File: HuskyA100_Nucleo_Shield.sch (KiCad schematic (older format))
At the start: 16 parts, among them CN10 HEADER_17x2, CN7 HEADER_10x2, CN8 HEADER_8x2, CN9 HEADER_15x2, J1 Conn_01x03, J2 Conn_01x03, J3 Conn_01x04, J4 Conn_01x04

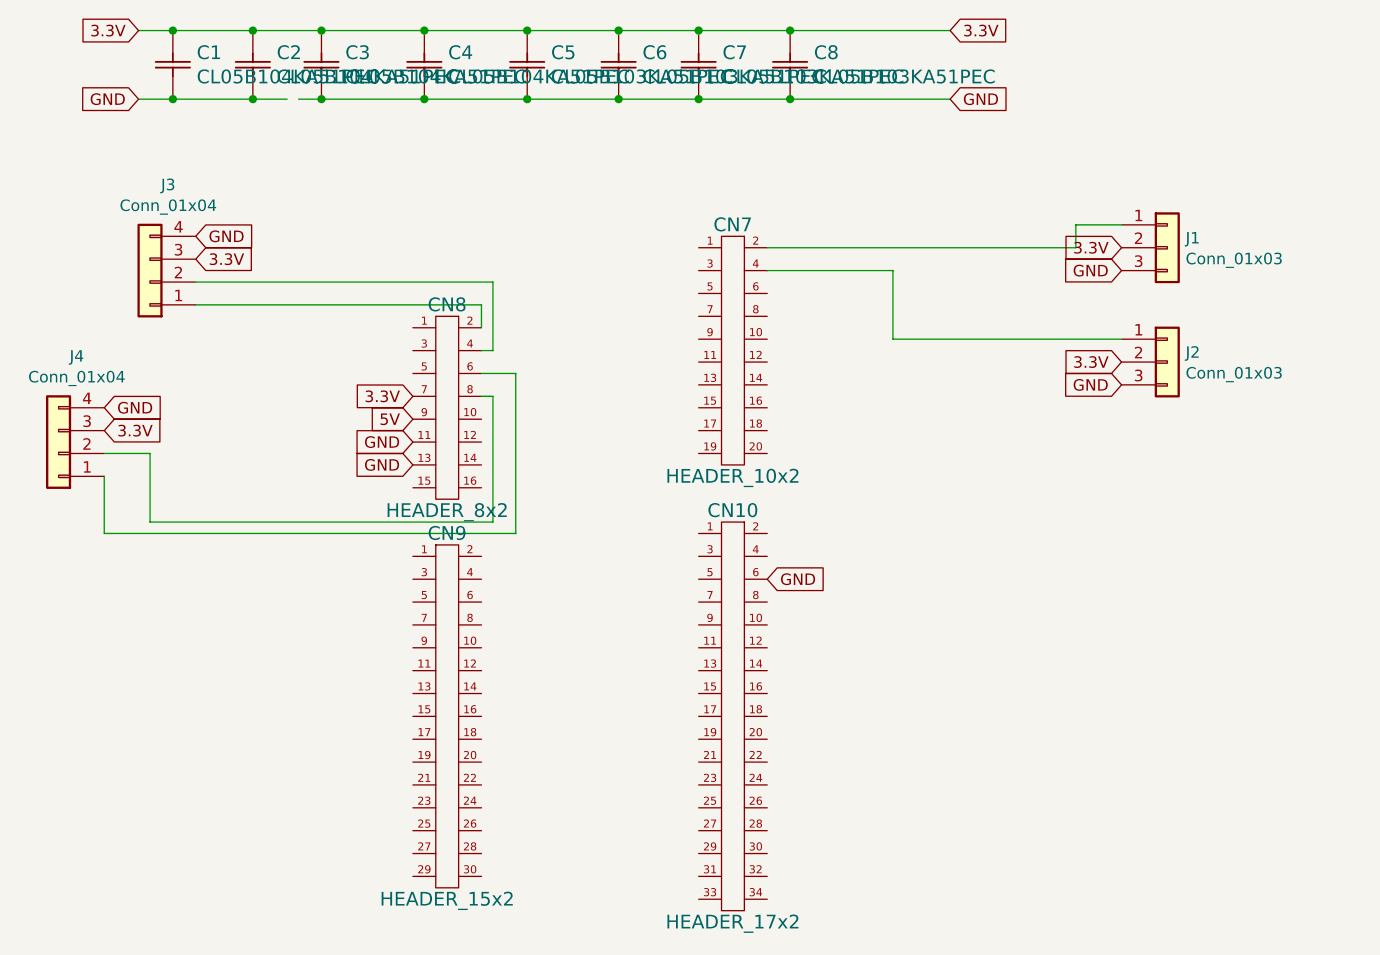
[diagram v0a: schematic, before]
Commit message: rerouted the pins to be correct in the schematic + deleted old traces
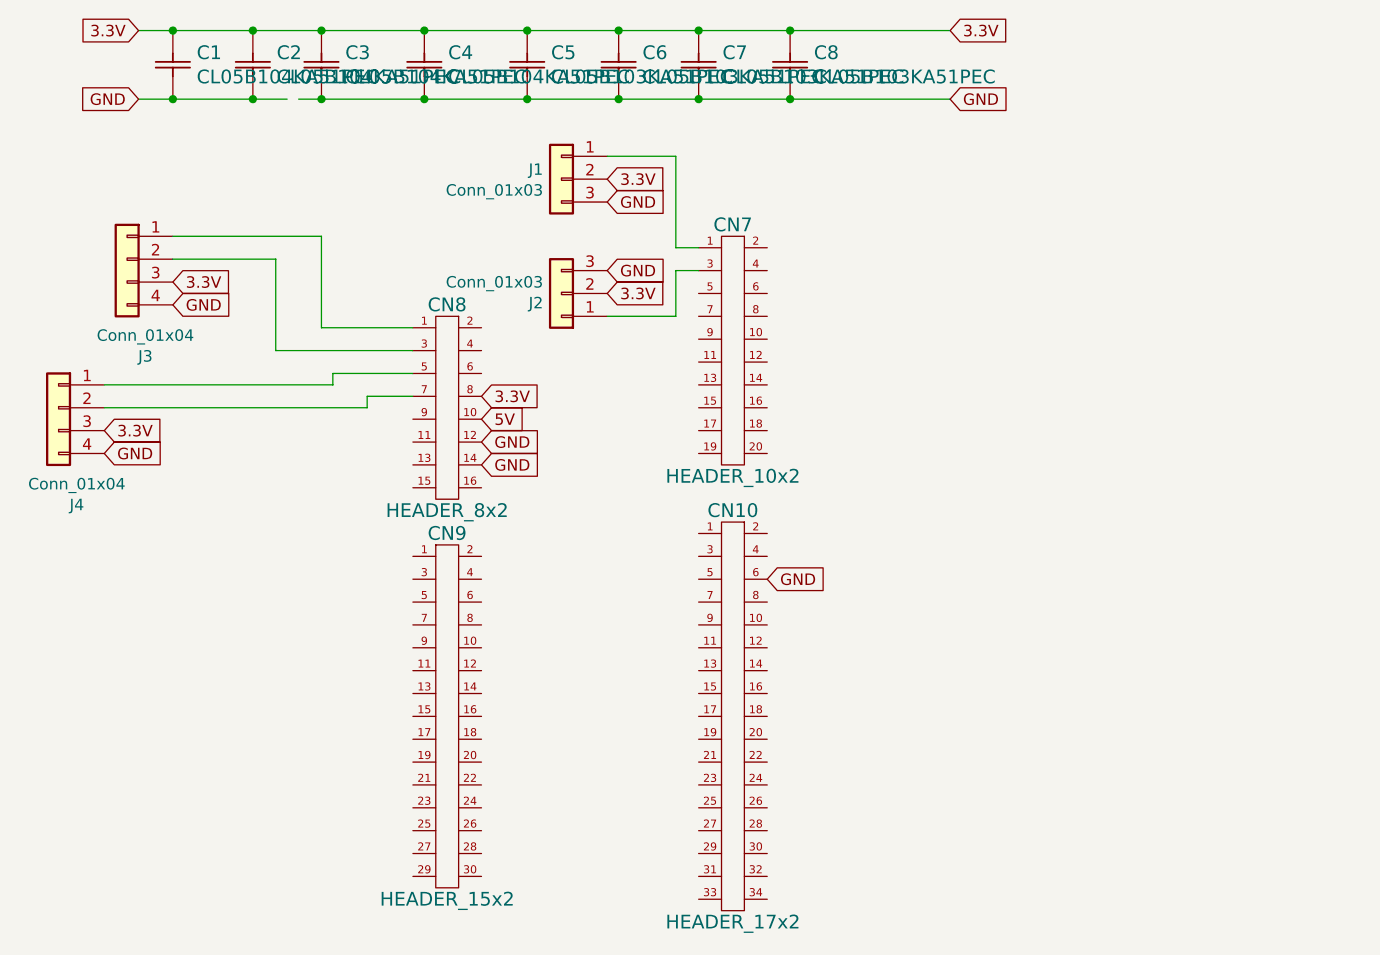
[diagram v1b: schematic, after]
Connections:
- wire segments 39 -> 37
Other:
- moved on the sheet: J1, J2, J3, J4
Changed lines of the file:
@@
 EESchema Schematic File Version 4
+LIBS:HuskyA100_Nucleo_Shield-cache
 EELAYER 26 0
 EELAYER END
@@
 L Connector_Generic:Conn_01x03 J1
 U 1 1 5C0735EF
-P 7450 3150
-F 0 "J1" H 7530 3192 50  0000 L CNN
-F 1 "Conn_01x03" H 7530 3101 50  0000 L CNN
-F 2 "Molex_Mini-Lock:Molex Mini-Lock Horizontal Header 3 circuit" H 7450 3150 50  0001 C CNN
-F 3 "~" H 7450 3150 50  0001 C CNN
-	1    7450 3150
-	1    0    0    -1
+P 4800 2850
+F 0 "J1" H 4880 2892 50  0000 L CNN
+F 1 "Conn_01x03" H 4880 2801 50  0000 L CNN
+F 2 "Molex_Mini-Lock:Molex Mini-Lock Horizontal Header 3 circuit" H 4800 2850 50  0001 C CNN
+F 3 "~" H 4800 2850 50  0001 C CNN
+	1    4800 2850
+	-1   0    0    -1
 $EndComp
 $Comp
 L Connector_Generic:Conn_01x03 J2
 U 1 1 5C0737C1
-P 7450 3650
-F 0 "J2" H 7530 3692 50  0000 L CNN
-F 1 "Conn_01x03" H 7530 3601 50  0000 L CNN
-F 2 "Molex_Mini-Lock:Molex Mini-Lock Horizontal Header 3 circuit" H 7450 3650 50  0001 C CNN
-F 3 "~" H 7450 3650 50  0001 C CNN
-	1    7450 3650
-	1    0    0    -1
+P 4800 3350
+F 0 "J2" H 4880 3392 50  0000 L CNN
+F 1 "Conn_01x03" H 4880 3301 50  0000 L CNN
+F 2 "Molex_Mini-Lock:Molex Mini-Lock Horizontal Header 3 circuit" H 4800 3350 50  0001 C CNN
+F 3 "~" H 4800 3350 50  0001 C CNN
+	1    4800 3350
+	-1   0    0    1
 $EndComp
 $Comp
 L Connector_Generic:Conn_01x04 J3
 U 1 1 5C073803
-P 3000 3300
-F 0 "J3" H 2920 2875 50  0000 C CNN
-F 1 "Conn_01x04" H 2920 2966 50  0000 C CNN
-F 2 "Molex_Mini-Lock:Molex Mini-Lock Horizontal Header 4 circuit" H 3000 3300 50  0001 C CNN
-F 3 "~" H 3000 3300 50  0001 C CNN
-	1    3000 3300
-	-1   0    0    1
+P 2900 3200
+F 0 "J3" H 2820 2775 50  0000 C CNN
+F 1 "Conn_01x04" H 2820 2866 50  0000 C CNN
+F 2 "Molex_Mini-Lock:Molex Mini-Lock Horizontal Header 4 circuit" H 2900 3200 50  0001 C CNN
+F 3 "~" H 2900 3200 50  0001 C CNN
+	1    2900 3200
+	-1   0    0    -1
 $EndComp
 $Comp
 L Connector_Generic:Conn_01x04 J4
 U 1 1 5C073BBE
-P 2600 4050
-F 0 "J4" H 2520 3625 50  0000 C CNN
-F 1 "Conn_01x04" H 2520 3716 50  0000 C CNN
-F 2 "Molex_Mini-Lock:Molex Mini-Lock Horizontal Header 4 circuit" H 2600 4050 50  0001 C CNN
-F 3 "~" H 2600 4050 50  0001 C CNN
-	1    2600 4050
-	-1   0    0    1
-$EndComp
-Wire Wire Line
-	4450 3500 4450 3400
-Wire Wire Line
-	4450 3400 3200 3400
-Wire Wire Line
-	4500 3600 4500 3300
-Wire Wire Line
-	4500 3300 3200 3300
-Wire Wire Line
-	4500 3600 4450 3600
-Wire Wire Line
-	4450 3700 4600 3700
-Wire Wire Line
-	4450 3800 4500 3800
-Wire Wire Line
-	3000 4050 2800 4050
-Wire Wire Line
-	2800 4150 2800 4400
-Wire Wire Line
-	3000 4050 3000 4350
-Wire Wire Line
-	5700 3150 7050 3150
-Wire Wire Line
-	7050 3150 7050 3050
-Wire Wire Line
-	7050 3050 7250 3050
-Wire Wire Line
-	7250 3550 6250 3550
-Wire Wire Line
-	6250 3550 6250 3250
-Wire Wire Line
-	6250 3250 5700 3250
-Wire Wire Line
-	4500 4350 4500 3800
-Wire Wire Line
-	3000 4350 4500 4350
-Wire Wire Line
-	4600 4400 4600 3700
-Wire Wire Line
-	2800 4400 4600 4400
-Text GLabel 4150 3900 0    50   Input ~ 0
+P 2600 3850
+F 0 "J4" H 2520 3425 50  0000 C CNN
+F 1 "Conn_01x04" H 2520 3516 50  0000 C CNN
+F 2 "Molex_Mini-Lock:Molex Mini-Lock Horizontal Header 4 circuit" H 2600 3850 50  0001 C CNN
+F 3 "~" H 2600 3850 50  0001 C CNN
+	1    2600 3850
+	-1   0    0    -1
+$EndComp
+Text GLabel 4450 3900 2    50   Input ~ 0
 5V
-Text GLabel 4150 4000 0    50   Input ~ 0
-GND
-Text GLabel 4150 4100 0    50   Input ~ 0
-GND
-Text GLabel 4150 3800 0    50   Input ~ 0
+Text GLabel 4450 4000 2    50   Input ~ 0
+GND
+Text GLabel 4450 4100 2    50   Input ~ 0
+GND
+Text GLabel 4450 3800 2    50   Input ~ 0
 3.3V
 Text GLabel 2800 3950 2    50   Input ~ 0
 3.3V
-Text GLabel 3200 3200 2    50   Input ~ 0
-3.3V
-Text GLabel 7250 3750 0    50   Input ~ 0
-GND
-Text GLabel 7250 3250 0    50   Input ~ 0
-GND
-Text GLabel 7250 3150 0    50   Input ~ 0
-3.3V
-Text GLabel 7250 3650 0    50   Input ~ 0
-3.3V
-Text GLabel 3200 3100 2    50   Input ~ 0
-GND
-Text GLabel 2800 3850 2    50   Input ~ 0
+Text GLabel 3100 3300 2    50   Input ~ 0
+3.3V
+Text GLabel 5000 3250 2    50   Input ~ 0
+GND
+Text GLabel 5000 3350 2    50   Input ~ 0
+3.3V
+Text GLabel 3100 3400 2    50   Input ~ 0
+GND
+Text GLabel 2800 4050 2    50   Input ~ 0
 GND
 Text GLabel 5700 4600 2    50   Input ~ 0
@@
 Wire Wire Line
 	5800 2500 6500 2500
+Wire Wire Line
+	2800 3750 3800 3750
+Wire Wire Line
+	3800 3700 4150 3700
+Wire Wire Line
+	3950 3800 4150 3800
+Wire Wire Line
+	2800 3850 3950 3850
+Wire Wire Line
+	3950 3800 3950 3850
+Wire Wire Line
+	3800 3700 3800 3750
+Wire Wire Line
+	3100 3200 3550 3200
+Wire Wire Line
+	3550 3200 3550 3600
+Wire Wire Line
+	3550 3600 4150 3600
+Wire Wire Line
+	4150 3500 3750 3500
+Wire Wire Line
+	3750 3500 3750 3100
+Wire Wire Line
+	3750 3100 3100 3100
+Text GLabel 5000 2850 2    50   Input ~ 0
+3.3V
+Text GLabel 5000 2950 2    50   Input ~ 0
+GND
+Wire Wire Line
+	5000 2750 5300 2750
+Wire Wire Line
+	5300 2750 5300 3150
+Wire Wire Line
+	5300 3150 5400 3150
+Wire Wire Line
+	5000 3450 5300 3450
+Wire Wire Line
+	5300 3450 5300 3250
+Wire Wire Line
+	5300 3250 5400 3250
 $EndSCHEMATC

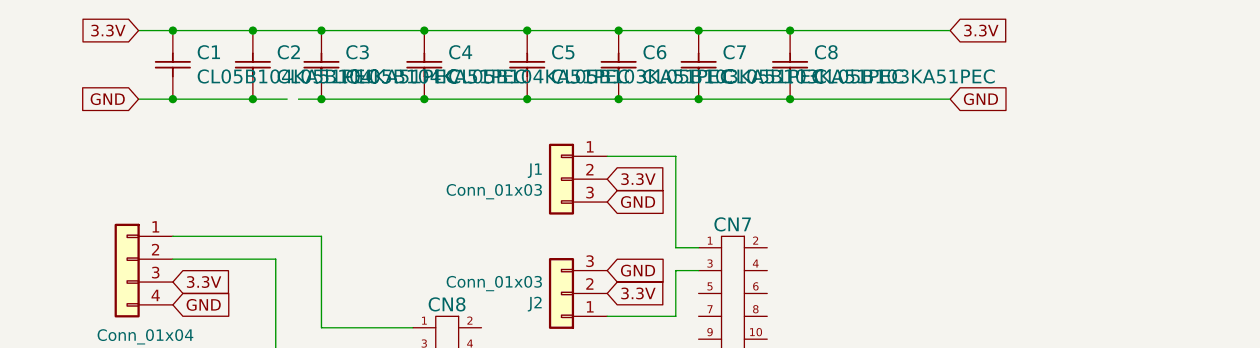
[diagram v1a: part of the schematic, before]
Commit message: Fixed #3 - replaced bypass caps with 5.6mm x 5.0mm case size to make them more easiy solderable
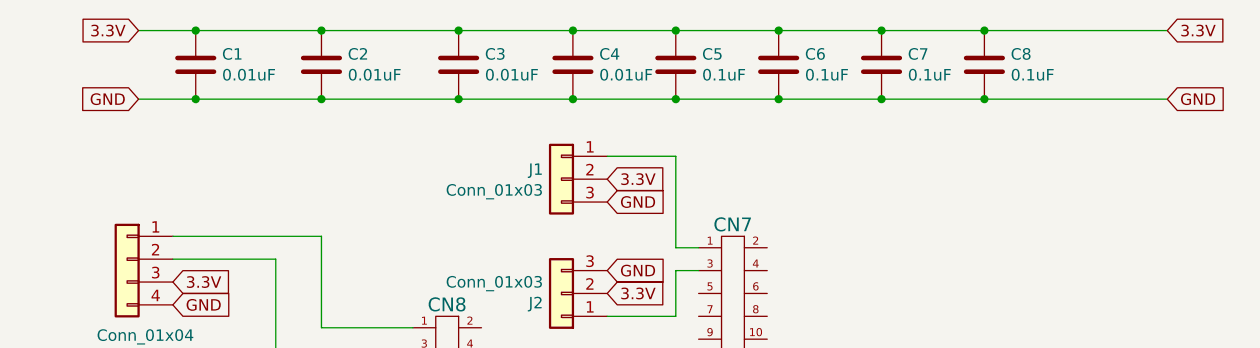
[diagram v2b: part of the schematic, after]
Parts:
- removed C1, C2, C3, C4: CL05B104KA51PEC, CL05B104KA51PEC:CL05B104KA51PEC, symbol CL05B104KA51PEC:CL05B104KA51PEC
- removed C5, C6, C7, C8: CL05B103KA51PEC, footprints:CL05B103KA51PEC, symbol symbols:CL05B103KA51PEC
- added C1, C2, C3, C4: 0.01uF, Capacitor_SMD:C_2220_5650Metric, symbol Device:C
- added C5, C6, C7, C8: 0.1uF, Capacitor_SMD:C_2220_5650Metric, symbol Device:C
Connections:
- wire segments 37 -> 36
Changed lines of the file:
@@
 Text GLabel 5700 4600 2    50   Input ~ 0
 GND
-Text GLabel 6500 2200 2    50   Input ~ 0
+Text GLabel 7450 2200 2    50   Input ~ 0
 3.3V
 Text GLabel 2950 2200 0    50   Input ~ 0
 3.3V
-Text GLabel 6500 2500 2    50   Input ~ 0
+Text GLabel 7450 2500 2    50   Input ~ 0
 GND
 Text GLabel 2950 2500 0    50   Input ~ 0
 GND
-Wire Wire Line
-	3650 2500 3750 2500
-Wire Wire Line
-	2950 2200 3100 2200
-Wire Wire Line
-	2950 2500 3100 2500
-$Comp
-L CL05B104KA51PEC:CL05B104KA51PEC C1
-U 1 1 5C4705DA
-P 3100 2200
-F 0 "C1" V 3197 2304 60  0000 L CNN
-F 1 "CL05B104KA51PEC" V 3303 2304 60  0000 L CNN
-F 2 "CL05B104KA51PEC:CL05B104KA51PEC" H 3250 1840 60  0001 C CNN
-F 3 "" H 3100 2200 60  0000 C CNN
-	1    3100 2200
-	0    1    1    0
-$EndComp
-Connection ~ 3100 2200
-Wire Wire Line
-	3100 2200 3450 2200
-Connection ~ 3100 2500
-Wire Wire Line
-	3100 2500 3450 2500
-$Comp
-L CL05B104KA51PEC:CL05B104KA51PEC C2
-U 1 1 5C470A7F
-P 3450 2200
-F 0 "C2" V 3547 2304 60  0000 L CNN
-F 1 "CL05B104KA51PEC" V 3653 2304 60  0000 L CNN
-F 2 "CL05B104KA51PEC:CL05B104KA51PEC" H 3600 1840 60  0001 C CNN
-F 3 "" H 3450 2200 60  0000 C CNN
-	1    3450 2200
-	0    1    1    0
-$EndComp
-Connection ~ 3450 2200
-Wire Wire Line
-	3450 2200 3750 2200
-Connection ~ 3450 2500
-Wire Wire Line
-	3450 2500 3600 2500
-$Comp
-L CL05B104KA51PEC:CL05B104KA51PEC C3
-U 1 1 5C471196
-P 3750 2200
-F 0 "C3" V 3847 2304 60  0000 L CNN
-F 1 "CL05B104KA51PEC" V 3953 2304 60  0000 L CNN
-F 2 "CL05B104KA51PEC:CL05B104KA51PEC" H 3900 1840 60  0001 C CNN
-F 3 "" H 3750 2200 60  0000 C CNN
-	1    3750 2200
-	0    1    1    0
-$EndComp
-Connection ~ 3750 2200
-Wire Wire Line
-	3750 2200 4200 2200
-Connection ~ 3750 2500
-Wire Wire Line
-	3750 2500 4200 2500
-$Comp
-L CL05B104KA51PEC:CL05B104KA51PEC C4
-U 1 1 5C4719CD
-P 4200 2200
-F 0 "C4" V 4297 2304 60  0000 L CNN
-F 1 "CL05B104KA51PEC" V 4403 2304 60  0000 L CNN
-F 2 "CL05B104KA51PEC:CL05B104KA51PEC" H 4350 1840 60  0001 C CNN
-F 3 "" H 4200 2200 60  0000 C CNN
-	1    4200 2200
-	0    1    1    0
-$EndComp
-Connection ~ 4200 2200
-Wire Wire Line
-	4200 2200 4650 2200
-Connection ~ 4200 2500
-Wire Wire Line
-	4200 2500 4650 2500
-$Comp
-L symbols:CL05B103KA51PEC C5
-U 1 1 5C473070
-P 4650 2200
-F 0 "C5" V 4747 2304 60  0000 L CNN
-F 1 "CL05B103KA51PEC" V 4853 2304 60  0000 L CNN
-F 2 "footprints:CL05B103KA51PEC" H 4800 1840 60  0001 C CNN
-F 3 "" H 4650 2200 60  0000 C CNN
-	1    4650 2200
-	0    1    1    0
-$EndComp
-Connection ~ 4650 2200
-Wire Wire Line
-	4650 2200 5050 2200
-Connection ~ 4650 2500
-Wire Wire Line
-	4650 2500 5050 2500
-$Comp
-L symbols:CL05B103KA51PEC C6
-U 1 1 5C473160
-P 5050 2200
-F 0 "C6" V 5147 2304 60  0000 L CNN
-F 1 "CL05B103KA51PEC" V 5253 2304 60  0000 L CNN
-F 2 "footprints:CL05B103KA51PEC" H 5200 1840 60  0001 C CNN
-F 3 "" H 5050 2200 60  0000 C CNN
-	1    5050 2200
-	0    1    1    0
-$EndComp
-Connection ~ 5050 2200
-Wire Wire Line
-	5050 2200 5400 2200
-Connection ~ 5050 2500
-Wire Wire Line
-	5050 2500 5400 2500
-$Comp
-L symbols:CL05B103KA51PEC C7
-U 1 1 5C473DA9
-P 5400 2200
-F 0 "C7" V 5497 2304 60  0000 L CNN
-F 1 "CL05B103KA51PEC" V 5603 2304 60  0000 L CNN
-F 2 "footprints:CL05B103KA51PEC" H 5550 1840 60  0001 C CNN
-F 3 "" H 5400 2200 60  0000 C CNN
-	1    5400 2200
-	0    1    1    0
-$EndComp
-Connection ~ 5400 2200
-Wire Wire Line
-	5400 2200 5800 2200
-Connection ~ 5400 2500
-Wire Wire Line
-	5400 2500 5800 2500
-$Comp
-L symbols:CL05B103KA51PEC C8
-U 1 1 5C473E58
-P 5800 2200
-F 0 "C8" V 5897 2304 60  0000 L CNN
-F 1 "CL05B103KA51PEC" V 6003 2304 60  0000 L CNN
-F 2 "footprints:CL05B103KA51PEC" H 5950 1840 60  0001 C CNN
-F 3 "" H 5800 2200 60  0000 C CNN
-	1    5800 2200
-	0    1    1    0
-$EndComp
-Connection ~ 5800 2200
-Wire Wire Line
-	5800 2200 6500 2200
-Connection ~ 5800 2500
-Wire Wire Line
-	5800 2500 6500 2500
 Wire Wire Line
 	2800 3750 3800 3750
@@
 Wire Wire Line
 	5300 3250 5400 3250
+Wire Wire Line
+	2950 2200 3200 2200
+Wire Wire Line
+	2950 2500 3200 2500
+$Comp
+L Device:C C1
+U 1 1 5C66E788
+P 3200 2350
+F 0 "C1" H 3315 2396 50  0000 L CNN
+F 1 "0.01uF" H 3315 2305 50  0000 L CNN
+F 2 "Capacitor_SMD:C_2220_5650Metric" H 3238 2200 50  0001 C CNN
+F 3 "~" H 3200 2350 50  0001 C CNN
+	1    3200 2350
+	1    0    0    -1
+$EndComp
+Connection ~ 3200 2200
+Connection ~ 3200 2500
+$Comp
+L Device:C C2
+U 1 1 5C66E7DF
+P 3750 2350
+F 0 "C2" H 3865 2396 50  0000 L CNN
+F 1 "0.01uF" H 3865 2305 50  0000 L CNN
+F 2 "Capacitor_SMD:C_2220_5650Metric" H 3788 2200 50  0001 C CNN
+F 3 "~" H 3750 2350 50  0001 C CNN
+	1    3750 2350
+	1    0    0    -1
+$EndComp
+$Comp
+L Device:C C3
+U 1 1 5C66E843
+P 4350 2350
+F 0 "C3" H 4465 2396 50  0000 L CNN
+F 1 "0.01uF" H 4465 2305 50  0000 L CNN
+F 2 "Capacitor_SMD:C_2220_5650Metric" H 4388 2200 50  0001 C CNN
+F 3 "~" H 4350 2350 50  0001 C CNN
+	1    4350 2350
+	1    0    0    -1
+$EndComp
+$Comp
+L Device:C C4
+U 1 1 5C66E890
+P 4850 2350
+F 0 "C4" H 4965 2396 50  0000 L CNN
+F 1 "0.01uF" H 4965 2305 50  0000 L CNN
+F 2 "Capacitor_SMD:C_2220_5650Metric" H 4888 2200 50  0001 C CNN
+F 3 "~" H 4850 2350 50  0001 C CNN
+	1    4850 2350
+	1    0    0    -1
+$EndComp
+Connection ~ 3750 2200
+Connection ~ 3750 2500
+Connection ~ 4350 2200
+Connection ~ 4350 2500
+Wire Wire Line
+	3200 2200 3750 2200
+Wire Wire Line
+	3200 2500 3750 2500
+Wire Wire Line
+	3750 2200 4350 2200
+Wire Wire Line
+	3750 2500 4350 2500
+Connection ~ 4850 2200
+Wire Wire Line
+	4850 2200 5300 2200
+Connection ~ 4850 2500
+Wire Wire Line
+	4850 2500 5300 2500
+Wire Wire Line
+	4350 2200 4850 2200
+Wire Wire Line
+	4350 2500 4850 2500
+$Comp
+L Device:C C5
+U 1 1 5C6712DB
+P 5300 2350
+F 0 "C5" H 5415 2396 50  0000 L CNN
+F 1 "0.1uF" H 5415 2305 50  0000 L CNN
+F 2 "Capacitor_SMD:C_2220_5650Metric" H 5338 2200 50  0001 C CNN
+F 3 "~" H 5300 2350 50  0001 C CNN
+	1    5300 2350
+	1    0    0    -1
+$EndComp
+$Comp
+L Device:C C6
+U 1 1 5C671C26
+P 5750 2350
+F 0 "C6" H 5865 2396 50  0000 L CNN
+F 1 "0.1uF" H 5865 2305 50  0000 L CNN
+F 2 "Capacitor_SMD:C_2220_5650Metric" H 5788 2200 50  0001 C CNN
+F 3 "~" H 5750 2350 50  0001 C CNN
+	1    5750 2350
+	1    0    0    -1
+$EndComp
+$Comp
+L Device:C C7
+U 1 1 5C67202E
+P 6200 2350
+F 0 "C7" H 6315 2396 50  0000 L CNN
+F 1 "0.1uF" H 6315 2305 50  0000 L CNN
+F 2 "Capacitor_SMD:C_2220_5650Metric" H 6238 2200 50  0001 C CNN
+F 3 "~" H 6200 2350 50  0001 C CNN
+	1    6200 2350
+	1    0    0    -1
+$EndComp
+$Comp
+L Device:C C8
+U 1 1 5C672439
+P 6650 2350
+F 0 "C8" H 6765 2396 50  0000 L CNN
+F 1 "0.1uF" H 6765 2305 50  0000 L CNN
+F 2 "Capacitor_SMD:C_2220_5650Metric" H 6688 2200 50  0001 C CNN
+F 3 "~" H 6650 2350 50  0001 C CNN
+	1    6650 2350
+	1    0    0    -1
+$EndComp
+Connection ~ 5300 2200
+Connection ~ 5300 2500
+Connection ~ 5750 2200
+Wire Wire Line
+	5750 2200 6200 2200
+Connection ~ 5750 2500
+Wire Wire Line
+	5750 2500 6200 2500
+Wire Wire Line
+	5300 2200 5750 2200
+Wire Wire Line
+	5300 2500 5750 2500
+Connection ~ 6200 2200
+Wire Wire Line
+	6200 2200 6650 2200
+Connection ~ 6200 2500
+Wire Wire Line
+	6200 2500 6650 2500
+Connection ~ 6650 2200
+Wire Wire Line
+	6650 2200 7450 2200
+Connection ~ 6650 2500
+Wire Wire Line
+	6650 2500 7450 2500
 $EndSCHEMATC
